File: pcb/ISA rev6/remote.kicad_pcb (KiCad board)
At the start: 2 copper layers, 50 x 50 mm, 21 parts, among them J1 Remote Connector, J2 Generic Connector, J3 PiOLED Connector, J4 Qwiic/STEMMA QT, J5 User Controllable GPIO, SW1 Up, SW2 Down, SW3 Select, SW4 Back, U1 AMS1117-3.3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

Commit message: PCB rev 6 part deux
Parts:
- J1: value Remote Connector -> SATA RH Connector
- J5: value User Controllable GPIO -> Config Jumpers; footprint Connector_PinHeader_2.54mm:PinHeader_1x05_P2.54mm_Vertical -> modified ICs:2x03 solder jumper; moved to B.Cu
- moved J5 16.3 mm to (137.4, 76.5), turned to 180 degrees
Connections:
- J5 pad 2: Net-(J5-Pad2) -> +3V3
- J5 pad 3: Net-(J5-Pad3) -> Net-(U2-Pad14)
- J5 pad 5: GND -> Net-(U2-Pad15)
- U2 pad 14: Net-(J5-Pad2) -> Net-(U2-Pad14)
- U2 pad 15: Net-(J5-Pad3) -> Net-(U2-Pad15)
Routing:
- net Net-(J5-Pad2): track 52.9 -> 0.00 mm
- net Net-(J5-Pad3): track 52.8 -> 0.00 mm
- net Net-(U2-Pad15): track 0.00 -> 35.2 mm
- net Net-(U2-Pad14): track 0.00 -> 34.0 mm
- net +3V3: track 24.1 -> 50.2 mm, vias 5 -> 6
- net Net-(U2-Pad13): track 54.2 -> 32.9 mm
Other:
- board text added: "1 2 3"
- board text added: "Config Jumpers"
- board text added: "J5-1: Display Type Open - SSD1306 Closed - SH1106"
- board text added: "J5-2: Display Res Open - 128x32 Closed - 128x64"
- board text added: "PicoPOST I2C Remote v0.1 - 2023/01/01"
- board text removed: "GND 3v3 7 6 5"
- board text removed: "PicoPOST I2C Remote v0.1 - 2022/12/31"
- board text removed: "User Definable"

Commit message: final tweaks to rev6?
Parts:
- J1: value SATA RH Connector -> Remote Connector
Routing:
- net Net-(U2-Pad15): track 35.2 -> 33.1 mm
- net Net-(U2-Pad14): track 34.0 -> 32.3 mm
- net Net-(U2-Pad13): track 32.9 -> 31.8 mm
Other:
- board text added: "J5-3: Display Rotate Open - Normal Closed - Rotated"
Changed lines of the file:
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@@
     (property "Sheetname" "")
     (attr smd)
-    (fp_text reference "J4" (at 0 -3.98 90) (layer "F.SilkS")
+    (fp_text reference "J4" (at -5.08 0.254 180) (layer "F.SilkS")
       (effects (font (size 1 1) (thickness 0.15)))
     )
@@
     (property "Sheetname" "")
     (attr smd)
-    (fp_text reference "U1" (at 0 4.5 90) (layer "B.SilkS")
+    (fp_text reference "U1" (at -0.762 -5.08 180) (layer "B.SilkS")
       (effects (font (size 1 1) (thickness 0.15)) (justify mirror))
     )
@@
     (property "Sheetname" "")
     (attr smd)
-    (fp_text reference "R3" (at 0 1.82 90) (layer "B.SilkS")
+    (fp_text reference "R3" (at -3.302 0 180) (layer "B.SilkS")
       (effects (font (size 1 1) (thickness 0.15)) (justify mirror))
     )
@@
     (property "Sheetname" "")
     (attr smd)
-    (fp_text reference "C1" (at 0 2.032 90) (layer "B.SilkS")
+    (fp_text reference "C1" (at -3.81 0 180) (layer "B.SilkS")
       (effects (font (size 1 1) (thickness 0.15)) (justify mirror))
     )
@@
       (effects (font (size 1 1) (thickness 0.15)) (justify right mirror))
     )
-    (fp_text value "SATA RH Connector" (at 0 0) (layer "B.SilkS")
+    (fp_text value "Remote Connector" (at 0 0) (layer "B.SilkS")
       (effects (font (size 1.27 1.27) (thickness 0.15)) (justify mirror))
     )
@@
     (property "Sheetname" "")
     (attr smd)
-    (fp_text reference "U2" (at -0.127 -6.858 90) (layer "B.SilkS")
+    (fp_text reference "U2" (at -6.604 0 180) (layer "B.SilkS")
       (effects (font (size 1 1) (thickness 0.15)) (justify mirror))
     )
@@
   (gr_arc (start 150.114 83.058) (mid 149.370051 84.854051) (end 147.574 85.598) (layer "Edge.Cuts") (width 0.0381))
   (gr_arc (start 147.574 35.56) (mid 149.370051 36.303949) (end 150.114 38.1) (layer "Edge.Cuts") (width 0.0381))
-  (gr_text "J5-1: Display Type\nOpen - SSD1306\nClosed -  SH1106" (at 146.05 63.5 90) (layer "B.SilkS")
+  (gr_text "J5-1: Display Type\nOpen - SSD1306\nClosed -  SH1106" (at 147.828 52.832 90) (layer "B.SilkS")
     (effects (font (size 0.8128 0.8128) (thickness 0.1524)) (justify right mirror))
   )
@@
     (effects (font (size 0.8128 0.8128) (thickness 0.1524)) (justify mirror))
   )
-  (gr_text "J5-2: Display Res\nOpen - 128x32\nClosed - 128x64\n" (at 146.05 79.248 90) (layer "B.SilkS")
+  (gr_text "J5-3: Display Rotate\nOpen - Normal\nClosed - Rotated" (at 147.828 79.502 90) (layer "B.SilkS")
+    (effects (font (size 0.8128 0.8128) (thickness 0.1524)) (justify right mirror))
+  )
+  (gr_text "J5-2: Display Res\nOpen - 128x32\nClosed - 128x64\n" (at 147.828 65.278 90) (layer "B.SilkS")
     (effects (font (size 0.8128 0.8128) (thickness 0.1524)) (justify right mirror))
   )
@@
     (effects (font (size 1.27 1.27) (thickness 0.2)))
   )
-  (gr_text "Qwiic\n(StemmaQT)" (at 140.462 55.626 90) (layer "F.SilkS")
+  (gr_text "Qwiic\n(StemmaQT)" (at 141.224 55.626 90) (layer "F.SilkS")
     (effects (font (size 0.8128 0.8128) (thickness 0.1524)))
   )
@@
   (segment (start 117.856 82.55) (end 117.856 77.807) (width 0.127) (layer "B.Cu") (net 12))
   (segment (start 115.824 83.312) (end 117.094 83.312) (width 0.127) (layer "B.Cu") (net 12))
-  (segment (start 133.35 83.566) (end 133.35 77.3538) (width 0.127) (layer "B.Cu") (net 13))
+  (segment (start 112.776 82.804) (end 113.538 83.566) (width 0.127) (layer "B.Cu") (net 13))
+  (segment (start 133.35 77.3538) (end 133.35 82.804) (width 0.127) (layer "B.Cu") (net 13))
   (segment (start 135.5198 75.184) (end 136.1948 75.184) (width 0.127) (layer "B.Cu") (net 13))
-  (segment (start 114.3 84.328) (end 132.588 84.328) (width 0.127) (layer "B.Cu") (net 13))
+  (segment (start 112.776 81.358) (end 112.776 82.804) (width 0.127) (layer "B.Cu") (net 13))
   (segment (start 133.35 77.3538) (end 135.5198 75.184) (width 0.127) (layer "B.Cu") (net 13))
-  (segment (start 112.776 81.358) (end 112.776 82.804) (width 0.127) (layer "B.Cu") (net 13))
-  (segment (start 132.588 84.328) (end 133.35 83.566) (width 0.127) (layer "B.Cu") (net 13))
-  (segment (start 112.776 82.804) (end 114.3 84.328) (width 0.127) (layer "B.Cu") (net 13))
-  (segment (start 111.506 81.358) (end 111.506 83.058) (width 0.127) (layer "B.Cu") (net 14))
-  (segment (start 113.284 84.836) (end 133.096 84.836) (width 0.127) (layer "B.Cu") (net 14))
-  (segment (start 133.096 84.836) (end 133.858 84.074) (width 0.127) (layer "B.Cu") (net 14))
-  (segment (start 133.858 78.232) (end 135.636 76.454) (width 0.127) (layer "B.Cu") (net 14))
-  (segment (start 133.858 84.074) (end 133.858 78.232) (width 0.127) (layer "B.Cu") (net 14))
-  (segment (start 135.636 76.454) (end 136.1948 76.454) (width 0.127) (layer "B.Cu") (net 14))
-  (segment (start 111.506 83.058) (end 113.284 84.836) (width 0.127) (layer "B.Cu") (net 14))
-  (segment (start 112.776 85.344) (end 133.35 85.344) (width 0.127) (layer "B.Cu") (net 15))
+  (segment (start 133.35 82.804) (end 132.588 83.566) (width 0.127) (layer "B.Cu") (net 13))
+  (segment (start 113.538 83.566) (end 132.588 83.566) (width 0.127) (layer "B.Cu") (net 13))
+  (segment (start 133.858 78.232) (end 133.858 82.654531) (width 0.127) (layer "B.Cu") (net 14))
+  (segment (start 112.268 83.82) (end 111.506 83.058) (width 0.127) (layer "B.Cu") (net 14))
+  (segment (start 133.858 82.654531) (end 132.692531 83.82) (width 0.127) (layer "B.Cu") (net 14))
+  (segment (start 111.506 83.058) (end 111.506 81.358) (width 0.127) (layer "B.Cu") (net 14))
+  (segment (start 132.692531 83.82) (end 112.268 83.82) (width 0.127) (layer "B.Cu") (net 14))
+  (segment (start 136.1948 76.454) (end 135.636 76.454) (width 0.127) (layer "B.Cu") (net 14))
+  (segment (start 135.636 76.454) (end 133.858 78.232) (width 0.127) (layer "B.Cu") (net 14))
   (segment (start 134.874 77.724) (end 134.366 78.232) (width 0.127) (layer "B.Cu") (net 15))
-  (segment (start 133.35 85.344) (end 134.366 84.328) (width 0.127) (layer "B.Cu") (net 15))
-  (segment (start 110.236 81.358) (end 110.236 82.804) (width 0.127) (layer "B.Cu") (net 15))
+  (segment (start 134.366 82.505063) (end 132.797063 84.074) (width 0.127) (layer "B.Cu") (net 15))
   (segment (start 136.1948 77.724) (end 134.874 77.724) (width 0.127) (layer "B.Cu") (net 15))
-  (segment (start 110.236 82.804) (end 112.776 85.344) (width 0.127) (layer "B.Cu") (net 15))
-  (segment (start 134.366 84.328) (end 134.366 78.232) (width 0.127) (layer "B.Cu") (net 15))
+  (segment (start 110.236 82.804) (end 110.236 81.358) (width 0.127) (layer "B.Cu") (net 15))
+  (segment (start 134.366 78.232) (end 134.366 82.505063) (width 0.127) (layer "B.Cu") (net 15))
+  (segment (start 132.797063 84.074) (end 111.506 84.074) (width 0.127) (layer "B.Cu") (net 15))
+  (segment (start 111.506 84.074) (end 110.236 82.804) (width 0.127) (layer "B.Cu") (net 15))
   (zone (net 1) (net_name "+3V3") (layer "F.Cu") (name "front 3v3") (hatch edge 0.508)
     (connect_pads (clearance 0.508))

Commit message: final rev6 release
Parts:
- moved BZ1 0.76 mm to (98.9, 55.5)
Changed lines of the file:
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@@
   )
   (footprint "modified ICs:7.6mm side mount buzzer" (layer "B.Cu")
-    (at 98.1819 55.52455 180)
+    (at 98.9439 55.52455 180)
     (descr "tactile push button, 6x6mm e.g. PTS645xx series, height=9.5mm")
     (tags "tact sw push 6mm smd")

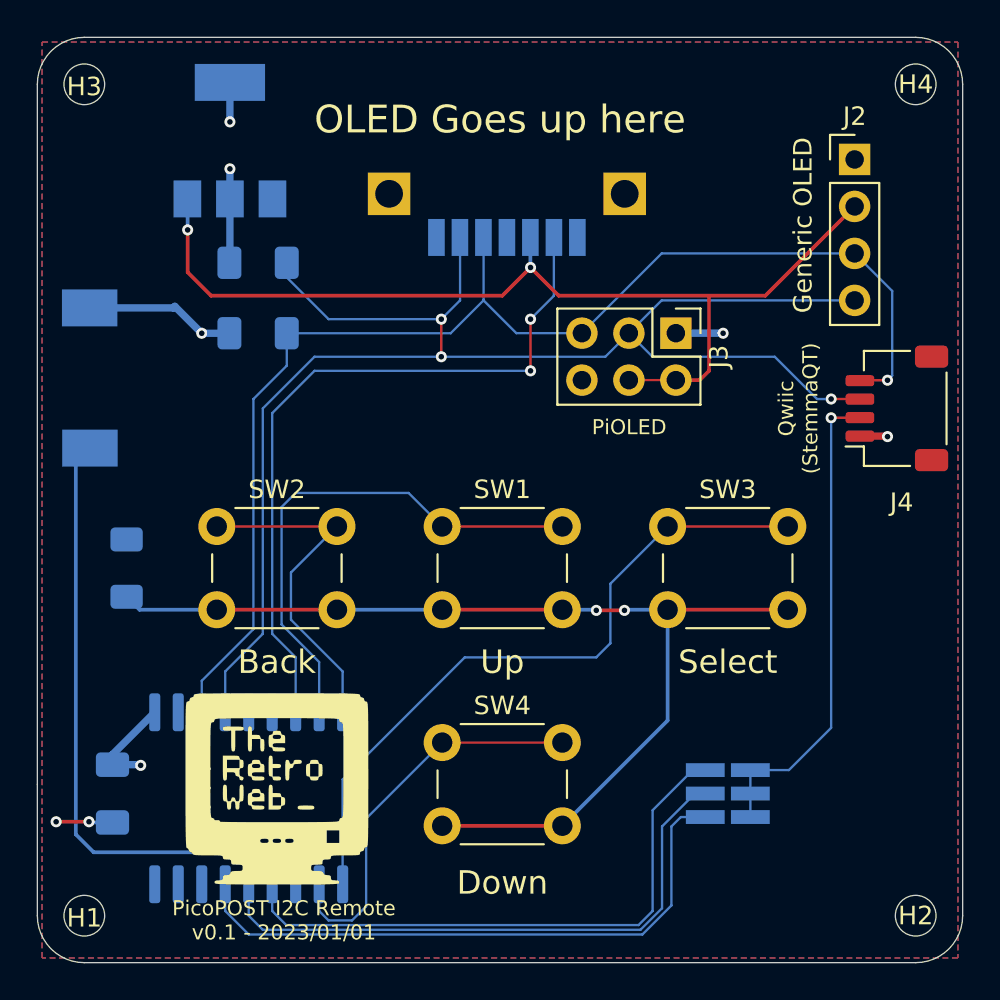
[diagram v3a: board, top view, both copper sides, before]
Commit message: [pcb] Fixed pinout mistake on remote connector
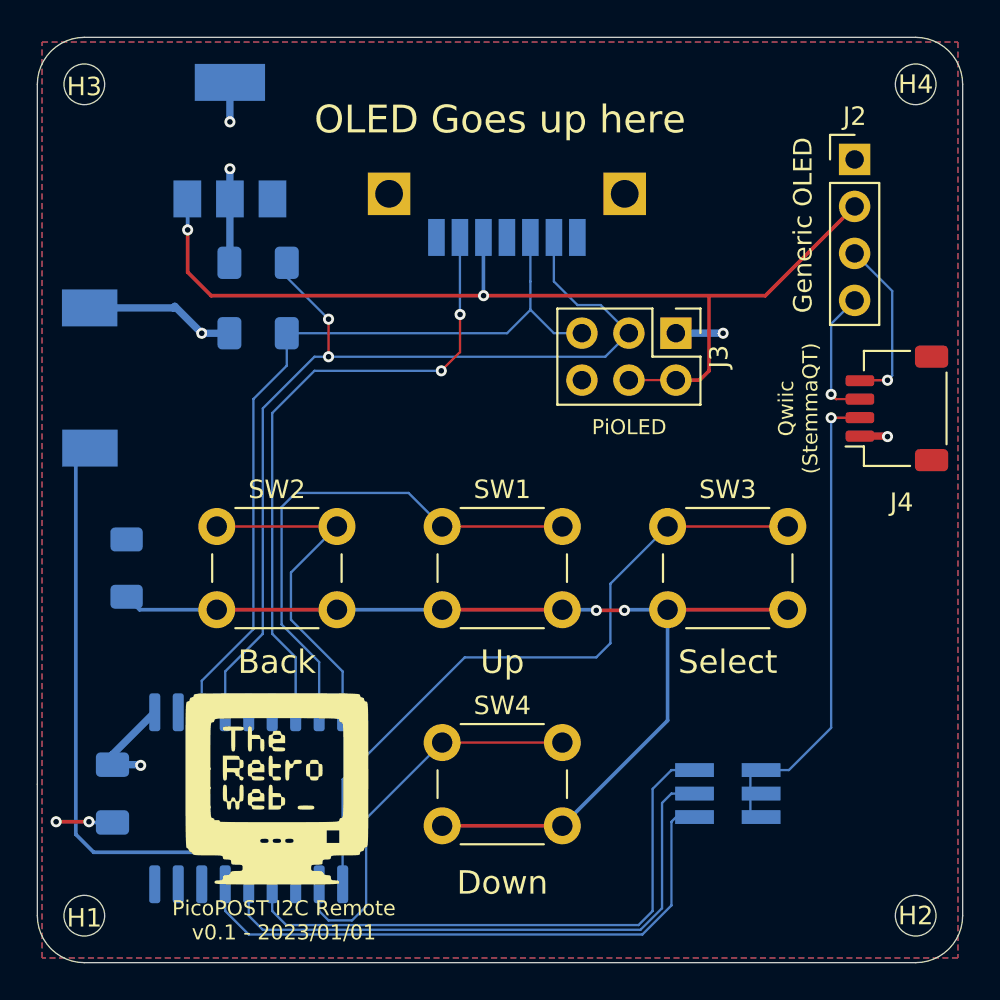
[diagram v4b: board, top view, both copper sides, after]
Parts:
- J1: value Remote Connector -> SATA RH Connector
- J5: footprint modified ICs:2x03 solder jumper -> Connector_PinSocket_1.27mm:PinSocket_2x03_P1.27mm_Vertical_SMD
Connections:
- J1 pad 2: /IRQ -> /SDA
- J1 pad 3: +5V -> /SCL
- J1 pad 5: /SCL -> +5V
- J1 pad 6: /SDA -> /IRQ
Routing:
- net /SDA: track 82.6 -> 59.6 mm
- net /SCL: track 69.1 -> 52.6 mm
- net /IRQ: track 39.4 -> 34.4 mm
- net +5V: track 54.1 -> 54.9 mm
- net Net-(J5-Pad3): track 32.3 -> 33.1 mm
- net Net-(J5-Pad1): track 31.8 -> 32.5 mm
